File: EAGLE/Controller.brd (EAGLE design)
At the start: 160 x 100 mm, 39 parts, among them IC1 TPS77033, IC2 TPS77033, Q1 200mA/40V, Q2 200mA/40V, Q3 2N3906, U1 ATMEGA328P_TQFP, U2 MCP73831, Y1 16MHz

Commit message: Pre Layout
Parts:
- removed Q1, Q2: 200mA/40V, SparkFun-DiscreteSemi:TO-92
- removed Q3: 2N3906, transistor-pnp:TO92
- removed R4: (no value), pot:B64Y
- added R11: (no value), pot-vitrohm:PC25
- added T1, T2: (no value), transistor-neu-to92:SOT23-BEC
- added T3: MMBT3906LT1SMD, transistor-pnp:SOT23-BEC
- moved R9 148.6 mm to (25.4, 85.1), turned to 180 degrees
- moved LED2 146.8 mm to (25.4, 88.9), turned to 90 degrees
- moved U1 142.2 mm to (-45.7, 7.62)
- moved TP2 140.9 mm to (16.5, 78.7)
- moved LED1 135.9 mm to (19.1, 88.9), turned to 90 degrees
- moved TP1 121.8 mm to (27.9, 76.2), flipped to the bottom
- moved R10 107.8 mm to (-34.3, 49.5), flipped to the bottom
- moved IC1 90.0 mm to (27.9, 86.4), flipped to the bottom
- moved U2 80.8 mm to (19.1, 81.3), turned to 90 degrees
- moved R1 78.2 mm to (20.3, 80.0), flipped to the bottom
- moved C10 77.0 mm to (19.1, 85.1), turned to 180 degrees
- moved C6 71.0 mm to (25.4, 86.4), flipped to the bottom, turned to 270 degrees
- moved C9 70.1 mm to (14.0, 85.1), turned to 270 degrees
- moved R7 64.7 mm to (14.0, 88.9), turned to 90 degrees
- moved R8 62.3 mm to (14.0, 81.3), turned to 90 degrees
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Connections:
- new net N$18: LED2.C, R9.1
- net GND: now also R11.A, T1.E, T2.E; no longer Q1.1, Q2.1, R4.A
- net N$1: now also T2.C, T3.B; no longer Q2.3, Q3.2
- net N$2: now also R11.S, T1.B; no longer Q1.2, R4.S
- net N$4: now also T1.C, T2.B, T3.C; no longer Q1.3, Q2.2, Q3.1
- net N$5: now also T3.E; no longer Q3.3
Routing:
- net N$1: track 0.00 -> 24.4 mm
- net N$14: track 0.00 -> 20.2 mm
- net VBAT: track 0.00 -> 18.9 mm
- net N$13: track 0.00 -> 16.8 mm
- net N$6: track 0.00 -> 13.5 mm
- net N$11: track 0.00 -> 10.9 mm
- net N$4: track 0.00 -> 9.87 mm
- net N$18: track 0.00 -> 4.16 mm
- net N$12: track 0.00 -> 3.82 mm
- net N$10: track 0.00 -> 3.73 mm
- net N$2: track 0.00 -> 3.31 mm
- net N$5: track 0.00 -> 2.08 mm
- net N$7: track 0.00 -> 1.78 mm

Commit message: pre-Layout
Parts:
- removed J2: (no value), SparkFun-Connectors:JST-2-SMD
- added C11, C12: 0.1uF, SparkFun-Capacitors:0603
- added FB4, FB5: 30Ω/1.8A, SparkFun-Coils:0603
- added JP1: (no value), pinhead:1X10/90
- added JP2: (no value), pinhead:1X04
- added JP3: (no value), pinhead:1X02/90
- moved U1 100.0 mm to (30.5, 72.4)
- moved LED3 94.0 mm to (22.9, 77.5), flipped to the top, turned to 90 degrees
- moved C3 83.0 mm to (25.4, 72.4), turned to 180 degrees
- moved C1 81.4 mm to (31.8, 71.1), turned to 90 degrees
- moved C2 80.1 mm to (25.4, 73.7), turned to 180 degrees
- moved FB3 69.3 mm to (21.6, 72.4), turned to 180 degrees
- moved R10 67.6 mm to (25.4, 81.3), flipped to the top, turned to 90 degrees
- moved FB2 65.6 mm to (21.6, 73.7), turned to 180 degrees
- moved FB1 59.9 mm to (21.6, 71.1), turned to 180 degrees
- moved Y1 55.3 mm to (22.9, 68.6), flipped to the top, turned to 270 degrees
- moved C8 54.0 mm to (16.5, 72.4)
- moved IC2 52.1 mm to (16.5, 69.8), turned to 90 degrees
- moved C6 9.92 mm to (31.8, 78.7), turned to 90 degrees
- moved IC1 7.73 mm to (29.2, 78.7), turned to 180 degrees
- moved T2 2.84 mm to (26.7, 82.5)
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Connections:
- removed net N$14: J2.2, S1.2
- removed net OELD_MOSI: U1.15
- removed net OLED_MISO: U1.16
- new net CAM_GND: C11.2, JP2.4
- new net CAM_VCC: C11.1, FB4.2, JP2.1
- new net LIPO_POS: JP3.1, S1.2
- new net OLED_DC: JP1.6, U1.12
- new net OLED_GND: C12.2, JP1.1
- new net OLED_MOSI: JP1.8, U1.15
- new net OLED_OC: JP1.4, U1.14
- new net OLED_RESET: JP1.5, U1.13
- new net OLED_VCC: C12.1, FB5.2, JP1.2
- net CAM_SCL: now also JP2.3
- net CAM_SDA: now also JP2.2
- net GND: now also JP3.2; no longer J2.1
- net N$8: now also FB4.1, FB5.1
- net OLED_SCK: now also JP1.7
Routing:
- net CAM_VCC: track 0.00 -> 34.6 mm
- net OLED_DC: track 0.00 -> 26.5 mm
- net OLED_MOSI: track 0.00 -> 25.1 mm, vias 0 -> 1
- net OLED_RESET: track 0.00 -> 21.9 mm, vias 0 -> 1
- net OLED_VCC: track 0.00 -> 21.0 mm
- net N$14: track 20.2 -> 0.00 mm
- net OLED_SCK: track 0.00 -> 17.8 mm
- net N$8: track 0.00 -> 17.6 mm, vias 0 -> 1
- net OLED_OC: track 0.00 -> 16.6 mm, vias 0 -> 1
- net CAM_SDA: track 0.00 -> 13.8 mm
- net CAM_SCL: track 0.00 -> 13.1 mm
- net AVCC: track 0.00 -> 13.1 mm, vias 0 -> 1
- net GND: track 0.00 -> 10.7 mm
- net VBAT: track 18.9 -> 29.5 mm
- net LIPO_POS: track 0.00 -> 9.42 mm
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- added copper zone on layer 1, net N$14
- added copper zone on layer 16, net N$20

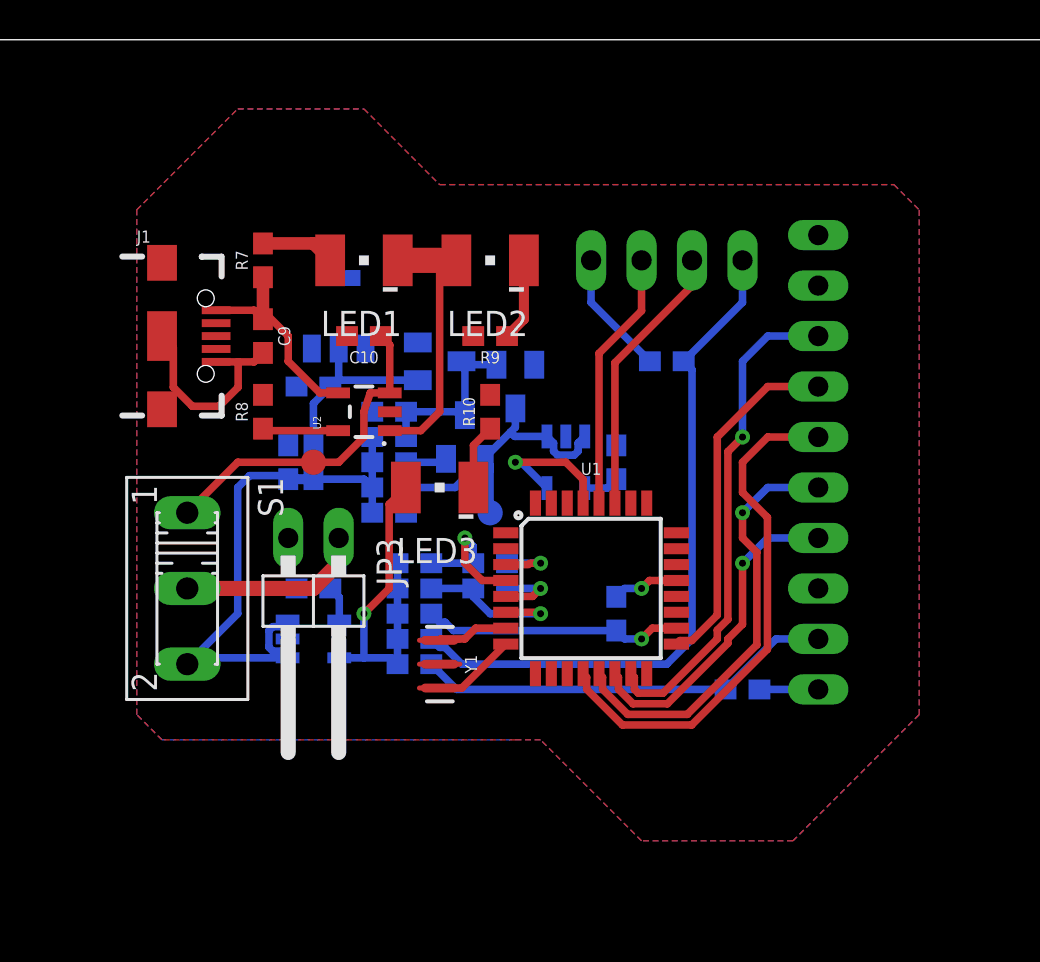
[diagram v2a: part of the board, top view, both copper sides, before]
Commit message: altered board to fit OSH DRS
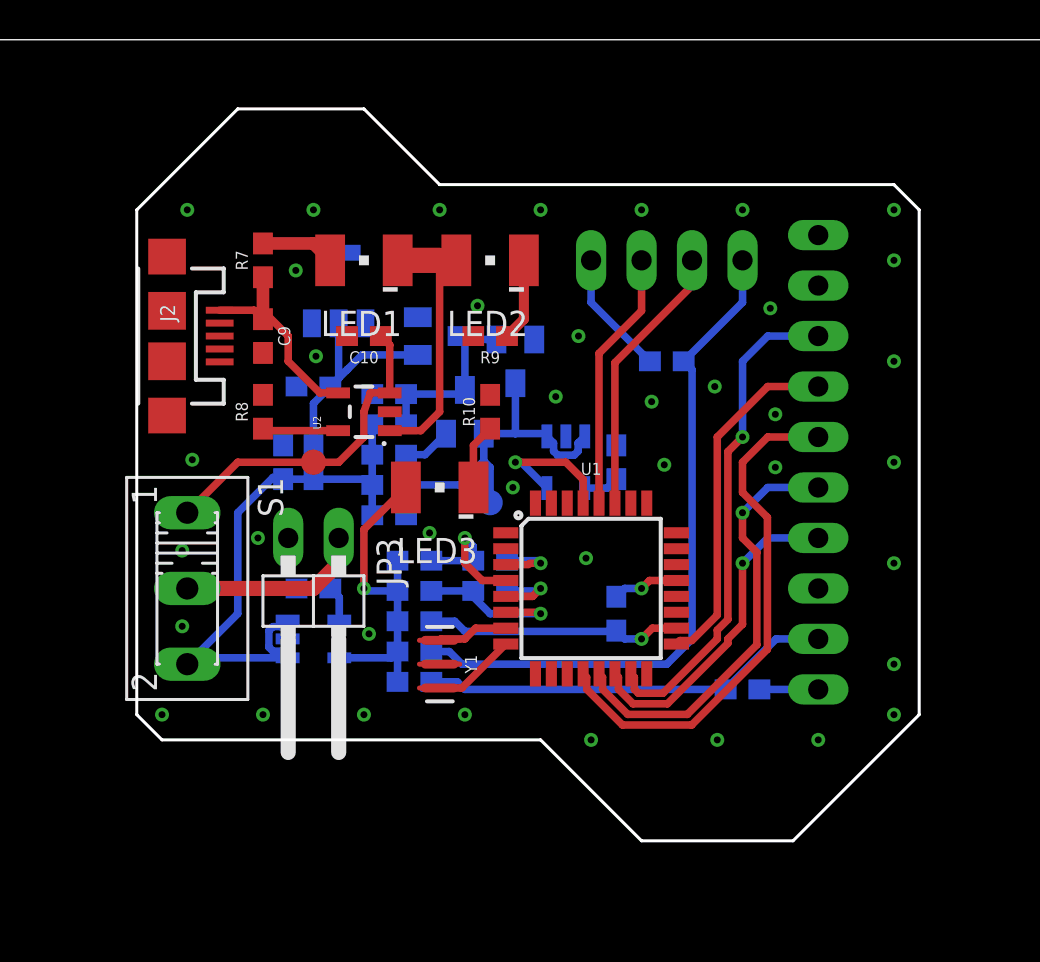
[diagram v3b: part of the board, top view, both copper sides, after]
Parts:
- removed J1: (no value), SparkFun-Connectors:USB-B-MICRO-SMD
- added J2: USB-MICROB, SparkFun-Retired:USB-MICROB
- moved T1 1.27 mm to (22.9, 85.1)
- moved R11 1.27 mm to (17.8, 87.6)
- moved T2 1.27 mm to (26.7, 83.8)
- moved T3 1.27 mm to (24.1, 81.3)
- moved C4 0.89 mm to (20.3, 82.2)
- moved FB5 0.89 mm to (21.6, 67.7)
- moved FB4 0.63 mm to (21.6, 69.2)
- moved R1 0.63 mm to (20.3, 80.6)
- moved TP1 0.51 mm to (25.4, 76.7)
- moved FB1 0.38 mm to (21.6, 70.7)
- moved R2 0.38 mm to (20.3, 79.1)
- moved C7 0.25 mm to (15.0, 78.7)
- moved C2 0.13 mm to (25.4, 73.8)
- moved FB2 0.13 mm to (21.6, 73.8)
- moved R3 0.13 mm to (20.3, 76.1)
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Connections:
- net GND: now also J2.GND, J2.MT1, J2.MT2; no longer J1.GND, J1.SHIELD1, J1.SHIELD2, J1.SHIELD3
- net N$11: now also J2.VBUS; no longer J1.VBUS
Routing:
- net GND: track 10.7 -> 0.00 mm, vias 0 -> 39
- net N$2: track 9.93 -> 12.2 mm
- net N$1: track 16.9 -> 18.5 mm
- net N$8: track 17.6 -> 16.9 mm
- added copper zone on layer 1, net GND
- added copper zone on layer 16, net GND
- removed copper zone on layer 1, net N$14
- removed copper zone on layer 16, net N$20
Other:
- outline, holes or cut-outs redrawn
